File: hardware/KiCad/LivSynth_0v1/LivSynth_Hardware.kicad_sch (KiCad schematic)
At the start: 0 parts

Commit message: Initial Routing finished
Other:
- sheet EG ports: added GATE_OUT; removed GATE_IN
- sheet IO ports: added ADC_IN1, ADC_IN2, CLOCK_OUT, RESET_OUT; removed ADC_OUT1, ADC_OUT2, CLOCK_IN, RESET_IN
- sheet MCU ports: added DAC_OUT1; removed DAC_OUT2
- sheet ModMatrix ports: added VCF_EG_OUT, VCF_LFO_OUT; removed VCF_CV_OUT
- sheet VCF ports: added VCF_CV1_IN, VCF_CV2_IN; removed VCF_EXP_CV_IN
- note added: "Todos: - Review Square Generator - check bypass caps - check IO connection security (add opamps and impedance resistors) - Check LED resistor values to get real white - Test status LED circuits - Check 1U Cap component format"
- note removed: "Todos: - Review Square Generator - check bypass caps - check IO connection security (add opamps and impedance resistors) - Check LED resistor values to get real white - Test status LED circuits"

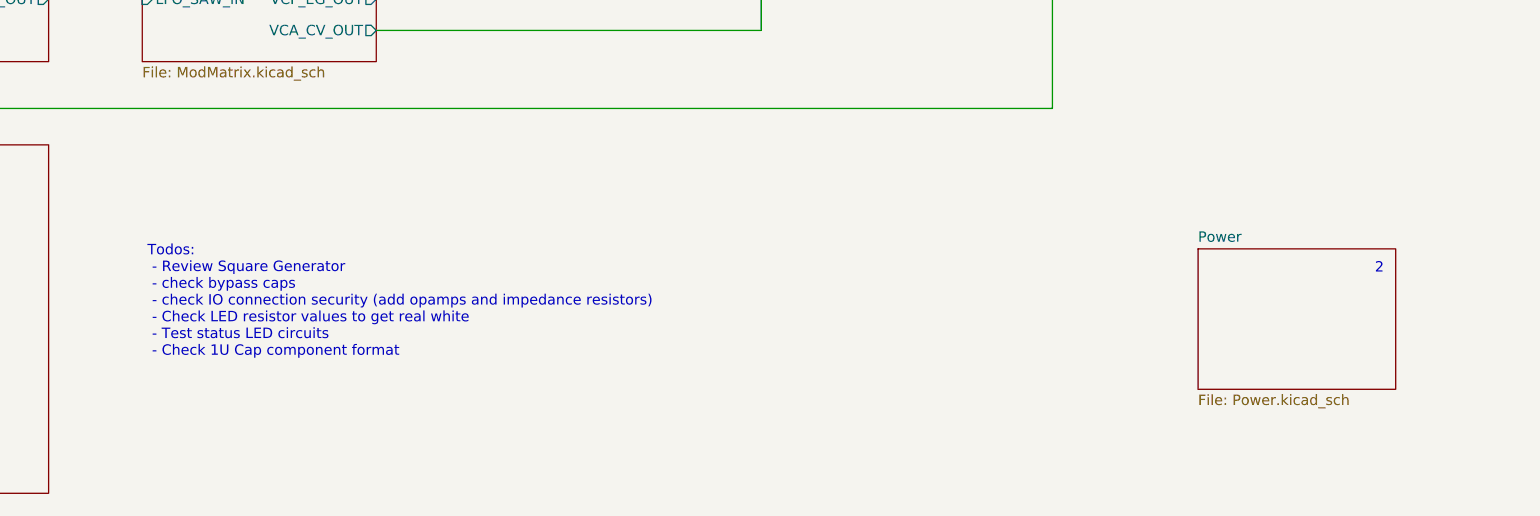
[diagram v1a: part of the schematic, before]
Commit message: Rework for polyester film capacitors
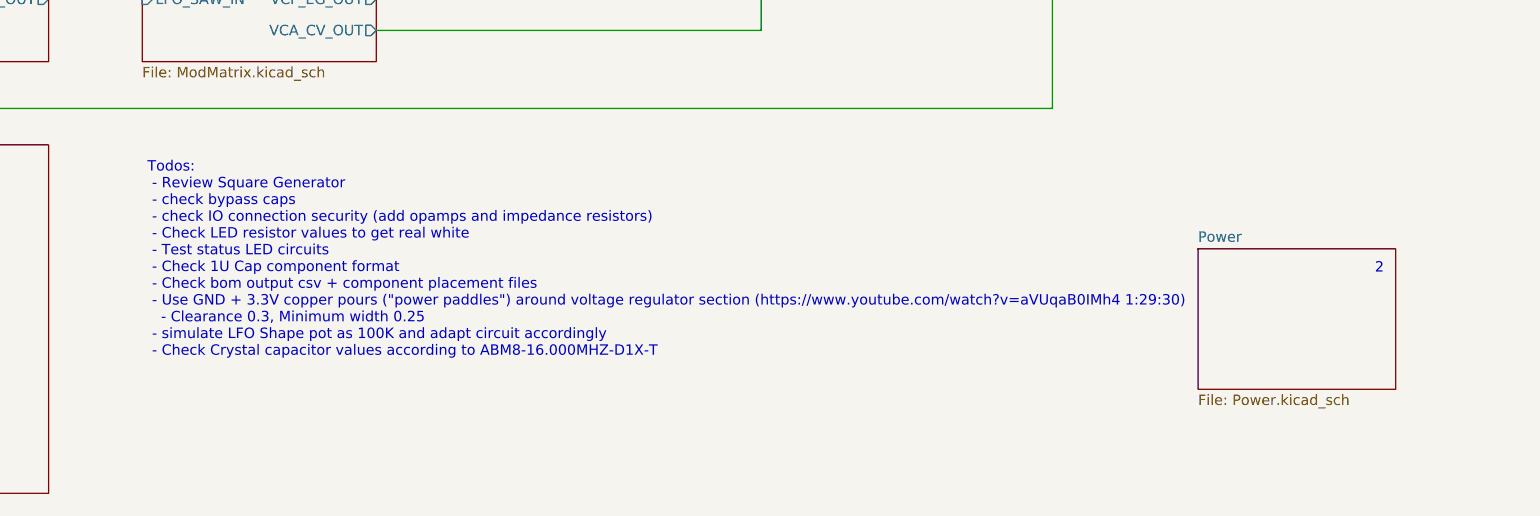
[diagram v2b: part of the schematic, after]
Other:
- note added: "Todos: - Review Square Generator - check bypass caps - check IO connection security (add opamps and impedance resistors) - Check LED resistor values to get real white - Test status LED circuits - Check 1U Cap component format - Check bom output csv + component placement files - Use GND + 3.3V copper pours ("power paddles") around voltage regulator section (https://www.youtube.com/watch?v=aVUqaB0I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"
- note removed: "Todos: - Review Square Generator - check bypass caps - check IO connection security (add opamps and impedance resistors) - Check LED resistor values to get real white - Test status LED circuits - Check 1U Cap component format"

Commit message: Change LED status circuits
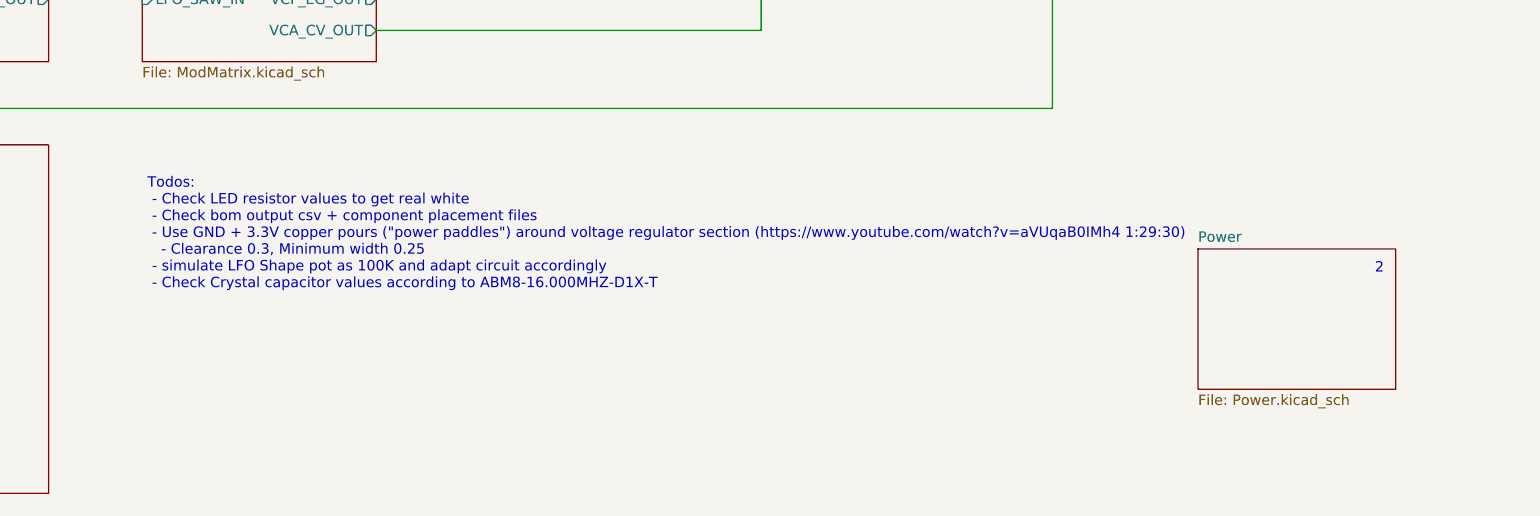
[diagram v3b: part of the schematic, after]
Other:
- note added: "Todos: - Check LED resistor values to get real white - Check bom output csv + component placement files - Use GND + 3.3V copper pours ("power paddles") around voltage regulator section (https://www.youtube.com/watch?v=aVUqaB0IMh4 1:29:30) - Clearance 0.3, Minimum width 0.25 - simulate LFO Shape pot as 100K and adapt circuit accordingly - Check Crystal capacitor values according to ABM8-16.000MHZ-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"
- note removed: "Todos: - Review Square Generator - check bypass caps - check IO connection security (add opamps and impedance resistors) - Check LED resistor values to get real white - Test status LED circuits - Check 1U Cap component format - Check bom output csv + component placement files - Use GND + 3.3V copper pours ("power paddles") around voltage regulator section (https://www.youtube.com/watch?v=aVUqaB0I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"
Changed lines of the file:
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@@
     (effects (font (size 1.27 1.27)) (justify left bottom))
   )
-  (text "Todos:\n - Review Square Generator\n - check bypass caps\n - check IO connection security (add opamps and impedance resistors)\n - Check LED resistor values to get real white\n - Test status LED circuits\n - Check 1U Cap component format\n - Check bom output csv + component placement files\n - Use GND + 3.3V copper pours (\"power paddles\") around voltage regulator section (https://www.youtube.com/watch?v=aVUqaB0IMh4 1:29:30)\n   - Clearance 0.3, Minimum width 0.25\n - simulate LFO Shape pot as 100K and adapt circuit accordingly\n - Check Crystal capacitor values according to ABM8-16.000MHZ-D1X-T"
-    (at 125.73 156.845 0)
+  (text "Todos:\n - Check LED resistor values to get real white\n - Check bom output csv + component placement files\n - Use GND + 3.3V copper pours (\"power paddles\") around voltage regulator section (https://www.youtube.com/watch?v=aVUqaB0IMh4 1:29:30)\n   - Clearance 0.3, Minimum width 0.25\n - simulate LFO Shape pot as 100K and adapt circuit accordingly\n - Check Crystal capacitor values according to ABM8-16.000MHZ-D1X-T"
+    (at 125.73 148.59 0)
     (effects (font (size 1.27 1.27)) (justify left bottom))
   )
@@
     )
     (path "/5bba0015-9baa-48b8-b961-e7169713a149/a120fd43-e4fa-457b-8799-55698c0147da"
-      (reference "J16") (unit 1) (value "IDC") (footprint "Capacitor_THT:C_Rect_L7.2mm_W2.5mm_P5.00mm_FKS2_FKP2_MKS2_MKP2")
+      (reference "J16") (unit 1) (value "IDC") (footprint "")
     )
     (path "/5bba0015-9baa-48b8-b961-e7169713a149/690645cc-ceed-495c-b456-6eef204f3560"
@@
     )
     (path "/5bba0015-9baa-48b8-b961-e7169713a149/79eb1d57-ba3c-4a77-a7c2-79d11b1f2eef"
-      (reference "LS1") (unit 1) (value "8R (<32R) 1W") (footprint "Capacitor_THT:C_Rect_L7.2mm_W2.5mm_P5.00mm_FKS2_FKP2_MKS2_MKP2")
+      (reference "LS1") (unit 1) (value "8R (<32R) 1W") (footprint "")
     )
     (path "/7456ffcb-9944-4baa-8068-78bd7ea392dc/10232e23-ee31-4051-88b4-9545104f4aad"
@@
     )
     (path "/a8e2a098-2010-4ec0-a897-f9a91ed4a45e/62c2da24-f56e-44f2-bb0c-43671340aecd"
-      (reference "R25") (unit 1) (value "10M") (footprint "Resistor_THT:R_Axial_DIN0207_L6.3mm_D2.5mm_P7.62mm_Horizontal")
+      (reference "R25") (unit 1) (value "1M") (footprint "Resistor_THT:R_Axial_DIN0207_L6.3mm_D2.5mm_P7.62mm_Horizontal")
     )
     (path "/a8e2a098-2010-4ec0-a897-f9a91ed4a45e/e9d792e4-983c-4f8c-8aae-e35c463d3e26"
@@
     )
     (path "/a8e2a098-2010-4ec0-a897-f9a91ed4a45e/e507c549-8eaa-4f64-9b6d-6c0e9b72953f"
-      (reference "R29") (unit 1) (value "10M") (footprint "Resistor_THT:R_Axial_DIN0207_L6.3mm_D2.5mm_P7.62mm_Horizontal")
+      (reference "R29") (unit 1) (value "1M") (footprint "Resistor_THT:R_Axial_DIN0207_L6.3mm_D2.5mm_P7.62mm_Horizontal")
     )
     (path "/a8e2a098-2010-4ec0-a897-f9a91ed4a45e/f1586601-0a56-497c-9ce8-fce4813bc07e"
-      (reference "R30") (unit 1) (value "2K") (footprint "Resistor_THT:R_Axial_DIN0207_L6.3mm_D2.5mm_P7.62mm_Horizontal")
+      (reference "R30") (unit 1) (value "1K") (footprint "Resistor_THT:R_Axial_DIN0207_L6.3mm_D2.5mm_P7.62mm_Horizontal")
     )
     (path "/a8e2a098-2010-4ec0-a897-f9a91ed4a45e/4f32a7c5-1d7b-4a20-af94-71ad0fe4cf45"
-      (reference "R31") (unit 1) (value "1K") (footprint "Resistor_THT:R_Axial_DIN0207_L6.3mm_D2.5mm_P7.62mm_Horizontal")
+      (reference "R31") (unit 1) (value "100R") (footprint "Resistor_THT:R_Axial_DIN0207_L6.3mm_D2.5mm_P7.62mm_Horizontal")
     )
     (path "/a8e2a098-2010-4ec0-a897-f9a91ed4a45e/1ed420c6-2ee1-44eb-b08b-25a4493a575f"
-      (reference "R32") (unit 1) (value "4K7") (footprint "Resistor_THT:R_Axial_DIN0207_L6.3mm_D2.5mm_P7.62mm_Horizontal")
+      (reference "R32") (unit 1) (value "1K") (footprint "Resistor_THT:R_Axial_DIN0207_L6.3mm_D2.5mm_P7.62mm_Horizontal")
     )
     (path "/c0ca57aa-71b4-4f05-9ee8-6e6126a36446/c2af18df-d836-482e-ba08-e0d8ec51dc1e"

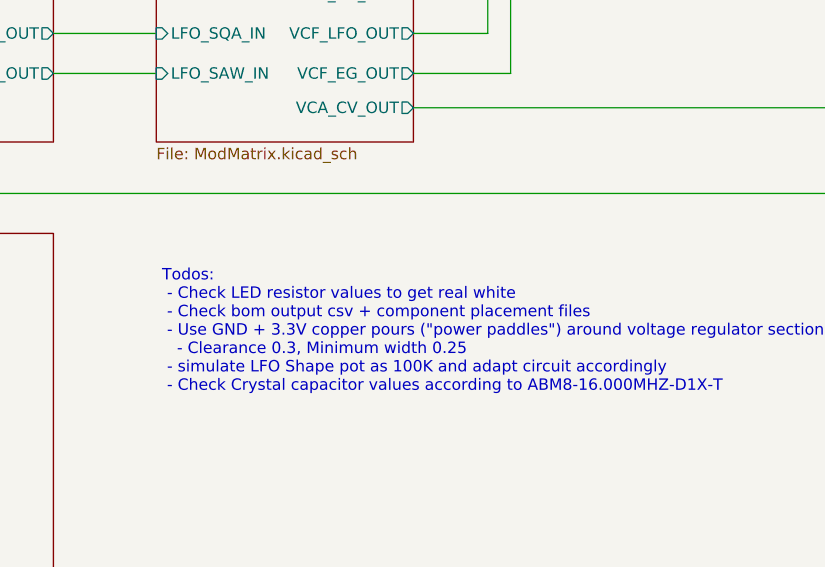
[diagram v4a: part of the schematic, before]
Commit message: White balance for RGB LEDs (update comments)
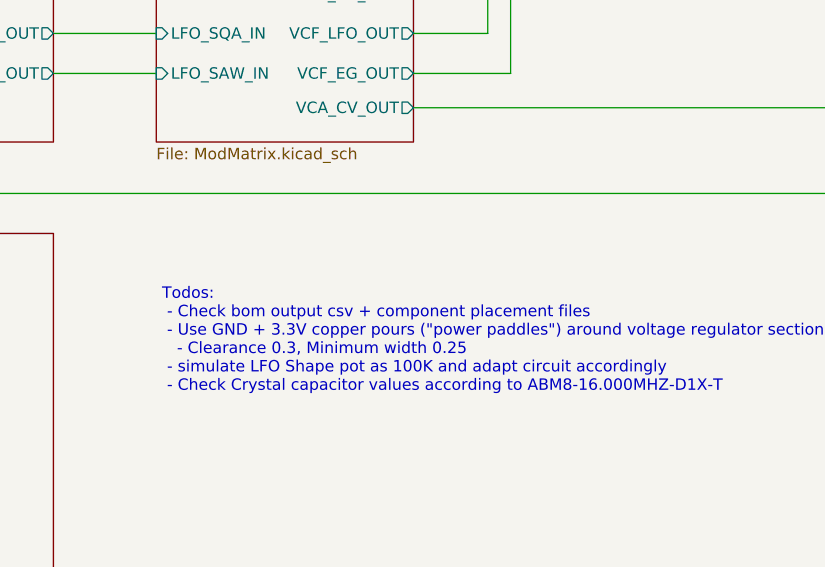
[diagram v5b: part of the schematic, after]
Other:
- note added: "Todos: - Check bom output csv + component placement files - Use GND + 3.3V copper pours ("power paddles") around voltage regulator section (https://www.youtube.com/watch?v=aVUqaB0IMh4 1:29:30) - Clearance 0.3, Minimum width 0.25 - simulate LFO Shape pot as 100K and adapt circuit accordingly - Check Crystal capacitor values according to ABM8-16.000MHZ-D1X-T"
- note removed: "Todos: - Check LED resistor values to get real white - Check bom output csv + component placement files - Use GND + 3.3V copper pours ("power paddles") around voltage regulator section (https://www.youtube.com/watch?v=aVUqaB0IMh4 1:29:30) - Clearance 0.3, Minimum width 0.25 - simulate LFO Shape pot as 100K and adapt circuit accordingly - Check Crystal capacitor values according to ABM8-16.000MHZ-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"
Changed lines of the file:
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@@
     (effects (font (size 1.27 1.27)) (justify left bottom))
   )
-  (text "Todos:\n - Check LED resistor values to get real white\n - Check bom output csv + component placement files\n - Use GND + 3.3V copper pours (\"power paddles\") around voltage regulator section (https://www.youtube.com/watch?v=aVUqaB0IMh4 1:29:30)\n   - Clearance 0.3, Minimum width 0.25\n - simulate LFO Shape pot as 100K and adapt circuit accordingly\n - Check Crystal capacitor values according to ABM8-16.000MHZ-D1X-T"
+  (text "Todos:\n - Check bom output csv + component placement files\n - Use GND + 3.3V copper pours (\"power paddles\") around voltage regulator section (https://www.youtube.com/watch?v=aVUqaB0IMh4 1:29:30)\n   - Clearance 0.3, Minimum width 0.25\n - simulate LFO Shape pot as 100K and adapt circuit accordingly\n - Check Crystal capacitor values according to ABM8-16.000MHZ-D1X-T"
     (at 125.73 148.59 0)
     (effects (font (size 1.27 1.27)) (justify left bottom))

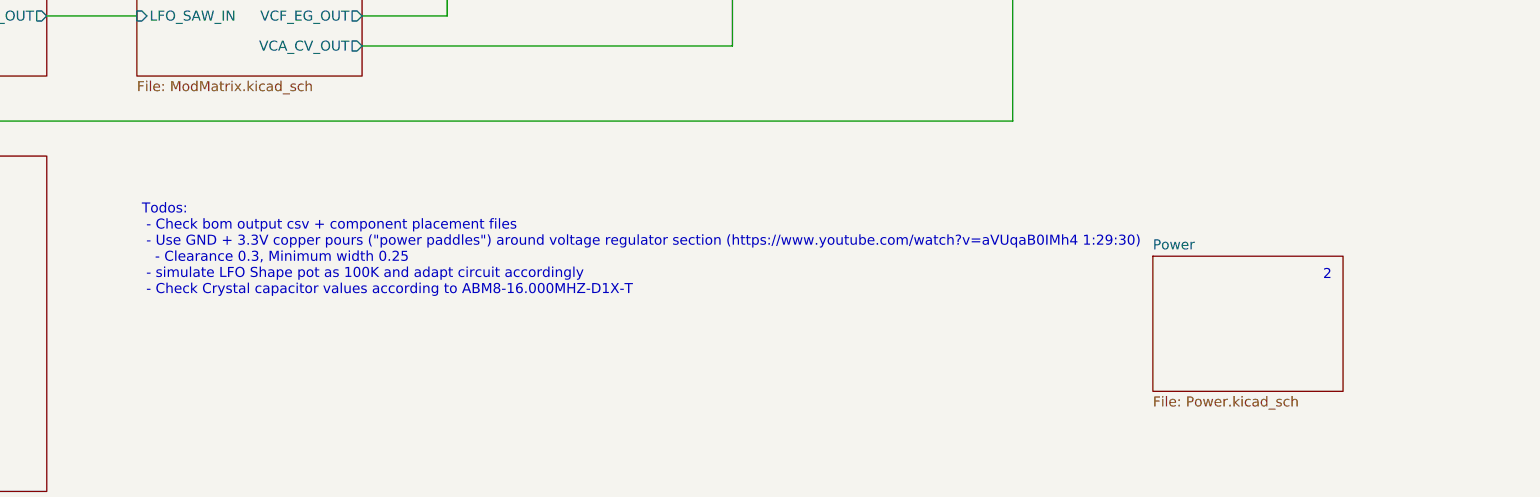
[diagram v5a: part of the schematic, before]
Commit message: Adjust crystal cap values Add BOM csv
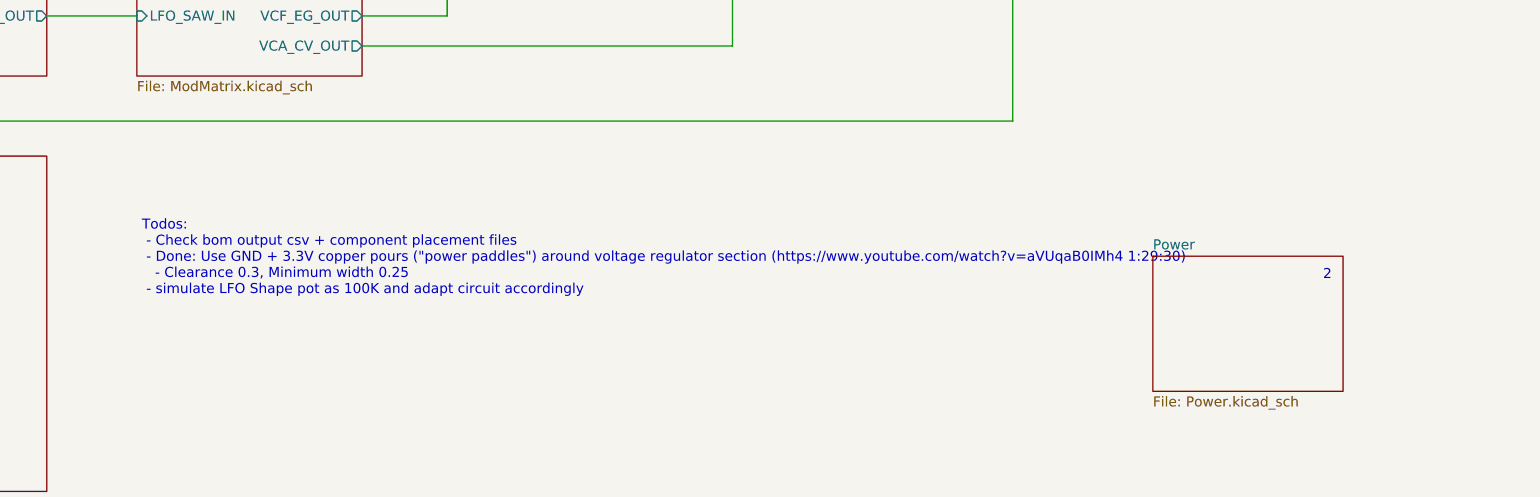
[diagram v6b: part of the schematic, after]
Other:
- note added: "Todos: - Check bom output csv + component placement files - Done: Use GND + 3.3V copper pours ("power paddles") around voltage regulator section (https://www.youtube.com/watch?v=aVUqaB0IMh4 1:29:30) - Clearance 0.3, Minimum width 0.25 - simulate LFO Shape pot as 100K and adapt circuit accordingly"
- note removed: "Todos: - Check bom output csv + component placement files - Use GND + 3.3V copper pours ("power paddles") around voltage regulator section (https://www.youtube.com/watch?v=aVUqaB0IMh4 1:29:30) - Clearance 0.3, Minimum width 0.25 - simulate LFO Shape pot as 100K and adapt circuit accordingly - Check Crystal capacitor values according to ABM8-16.000MHZ-D1X-T"
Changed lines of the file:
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@@
     (effects (font (size 1.27 1.27)) (justify left bottom))
   )
-  (text "Todos:\n - Check bom output csv + component placement files\n - Use GND + 3.3V copper pours (\"power paddles\") around voltage regulator section (https://www.youtube.com/watch?v=aVUqaB0IMh4 1:29:30)\n   - Clearance 0.3, Minimum width 0.25\n - simulate LFO Shape pot as 100K and adapt circuit accordingly\n - Check Crystal capacitor values according to ABM8-16.000MHZ-D1X-T"
+  (text "Todos:\n - Check bom output csv + component placement files\n - Done: Use GND + 3.3V copper pours (\"power paddles\") around voltage regulator section (https://www.youtube.com/watch?v=aVUqaB0IMh4 1:29:30)\n   - Clearance 0.3, Minimum width 0.25\n - simulate LFO Shape pot as 100K and adapt circuit accordingly"
     (at 125.73 148.59 0)
     (effects (font (size 1.27 1.27)) (justify left bottom))
@@
     )
     (path "/7456ffcb-9944-4baa-8068-78bd7ea392dc/e21e828c-6ff3-42b7-9a03-ab7fa8fd4a18"
-      (reference "C29") (unit 1) (value "16p") (footprint "Capacitor_SMD:C_0603_1608Metric_Pad1.08x0.95mm_HandSolder")
+      (reference "C29") (unit 1) (value "26p") (footprint "Capacitor_SMD:C_0603_1608Metric_Pad1.08x0.95mm_HandSolder")
     )
     (path "/7456ffcb-9944-4baa-8068-78bd7ea392dc/a3708aba-e02d-4d7a-93cc-9e27a6e07c83"
-      (reference "C30") (unit 1) (value "16p") (footprint "Capacitor_SMD:C_0603_1608Metric_Pad1.08x0.95mm_HandSolder")
+      (reference "C30") (unit 1) (value "26p") (footprint "Capacitor_SMD:C_0603_1608Metric_Pad1.08x0.95mm_HandSolder")
     )
     (path "/9b71f1c4-49e8-4b79-9df9-1d6c393fba92/1fbb261a-fa29-467e-9429-2a5861057524"
